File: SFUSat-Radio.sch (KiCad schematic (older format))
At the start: 11 parts, among them J1 SMA, J2 CONN-2POS-0.156\", P1 CONN_02X05, U1 2N7002DW

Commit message: added CC1101, fixed mission symbols
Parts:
- removed J2: CONN-2POS-0.156\", symbol CONN-2POS-0.156"
- added J3: PC104-8BIT, SFUSat:PC104-8bit, symbol PC104-8BIT
- added J4, J5, J6, J7: PC104PTH, SFUSat:PC104PTH, symbol PC104PTH
- D1, D2, D3: footprint SFUSat-Radio:LED_0603 -> SFUSat:LED_0603; symbol LED-RESCUE-SFUSat-Radio -> LED
- J1: footprint (none) -> SFUSat:SMA-Vert-TH
- R1, R2, R3: footprint (none) -> SFUSat:R_0402
- SW?1: footprint (none) -> SFUSat:1877285-2
- U1: footprint (none) -> SFUSat:SOT-363
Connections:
- wire segments 46 -> 52
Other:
- note added: "Need pull-up?\n"
- moved on the sheet: J1
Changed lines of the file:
@@
 F 0 "U1" H 6550 1350 60  0000 C CNN
 F 1 "2N7002DW" H 6350 1850 60  0000 C CNN
-F 2 "" H 6350 1600 60  0001 C CNN
+F 2 "SFUSat:SOT-363" H 6350 1600 60  0001 C CNN
 F 3 "" H 6350 1600 60  0000 C CNN
 	1    6350 1600
@@
 $EndComp
 $Comp
-L LED-RESCUE-SFUSat-Radio D1
+L LED D1
 U 1 1 587E94F9
 P 6950 1250
 F 0 "D1" H 6950 1350 50  0000 C CNN
 F 1 "GREEN" H 6950 1150 50  0000 C CNN
-F 2 "SFUSat-Radio:LED_0603" H 6950 1250 50  0001 C CNN
+F 2 "SFUSat:LED_0603" H 6950 1250 50  0001 C CNN
 F 3 "" H 6950 1250 50  0000 C CNN
 	1    6950 1250
@@
 F 0 "R1" V 7030 900 50  0000 C CNN
 F 1 "287" V 6950 900 50  0000 C CNN
-F 2 "" V 6880 900 50  0001 C CNN
+F 2 "SFUSat:R_0402" V 6880 900 50  0001 C CNN
 F 3 "" H 6950 900 50  0000 C CNN
 	1    6950 900
@@
 F 0 "R2" V 7330 900 50  0000 C CNN
 F 1 "287" V 7250 900 50  0000 C CNN
-F 2 "" V 7180 900 50  0001 C CNN
+F 2 "SFUSat:R_0402" V 7180 900 50  0001 C CNN
 F 3 "" H 7250 900 50  0000 C CNN
 	1    7250 900
@@
 $EndComp
 $Comp
-L LED-RESCUE-SFUSat-Radio D2
+L LED D2
 U 1 1 587EC634
 P 7250 1250
 F 0 "D2" H 7250 1350 50  0000 C CNN
 F 1 "RED" H 7250 1150 50  0000 C CNN
-F 2 "SFUSat-Radio:LED_0603" H 7250 1250 50  0001 C CNN
+F 2 "SFUSat:LED_0603" H 7250 1250 50  0001 C CNN
 F 3 "" H 7250 1250 50  0000 C CNN
 	1    7250 1250
@@
 $EndComp
 $Comp
-L GND #PWR01
+L GND #PWR8
 U 1 1 587EE6E2
 P 6800 1550
-F 0 "#PWR01" H 6800 1300 50  0001 C CNN
+F 0 "#PWR8" H 6800 1300 50  0001 C CNN
 F 1 "GND" H 6800 1400 50  0000 C CNN
 F 2 "" H 6800 1550 50  0000 C CNN
@@
 $EndComp
 $Comp
-L GND #PWR02
+L GND #PWR9
 U 1 1 587EE79C
 P 6800 1750
-F 0 "#PWR02" H 6800 1500 50  0001 C CNN
+F 0 "#PWR9" H 6800 1500 50  0001 C CNN
 F 1 "GND" H 6800 1600 50  0000 C CNN
 F 2 "" H 6800 1750 50  0000 C CNN
@@
 $EndComp
 $Comp
-L LED-RESCUE-SFUSat-Radio D3
+L LED D3
 U 1 1 587F1822
 P 7550 1250
 F 0 "D3" H 7550 1350 50  0000 C CNN
 F 1 "ORANGE" H 7550 1150 50  0000 C CNN
-F 2 "SFUSat-Radio:LED_0603" H 7550 1250 50  0001 C CNN
+F 2 "SFUSat:LED_0603" H 7550 1250 50  0001 C CNN
 F 3 "" H 7550 1250 50  0000 C CNN
 	1    7550 1250
@@
 F 0 "R3" V 7630 900 50  0000 C CNN
 F 1 "287" V 7550 900 50  0000 C CNN
-F 2 "" V 7480 900 50  0001 C CNN
+F 2 "SFUSat:R_0402" V 7480 900 50  0001 C CNN
 F 3 "" H 7550 900 50  0000 C CNN
 	1    7550 900
@@
 $EndComp
 $Comp
-L GND #PWR03
+L GND #PWR10
 U 1 1 587F1A5F
 P 7550 1450
-F 0 "#PWR03" H 7550 1200 50  0001 C CNN
+F 0 "#PWR10" H 7550 1200 50  0001 C CNN
 F 1 "GND" H 7550 1300 50  0000 C CNN
 F 2 "" H 7550 1450 50  0000 C CNN
@@
 L SMA J1
 U 1 1 5883A1B6
-P 9200 5050
-F 0 "J1" H 9400 4900 60  0000 C CNN
-F 1 "SMA" H 9400 5200 60  0000 C CNN
-F 2 "" H 9200 5050 60  0001 C CNN
-F 3 "" H 9200 5050 60  0000 C CNN
-	1    9200 5050
-	1    0    0    -1
-$EndComp
-$Comp
-L GND #PWR04
+P 9150 5100
+F 0 "J1" H 9350 4950 60  0000 C CNN
+F 1 "SMA" H 9350 5250 60  0000 C CNN
+F 2 "SFUSat:SMA-Vert-TH" H 9150 5100 60  0001 C CNN
+F 3 "" H 9150 5100 60  0000 C CNN
+	1    9150 5100
+	1    0    0    -1
+$EndComp
+$Comp
+L GND #PWR11
 U 1 1 5883A521
-P 9700 5050
-F 0 "#PWR04" H 9700 4800 50  0001 C CNN
-F 1 "GND" H 9700 4900 50  0000 C CNN
-F 2 "" H 9700 5050 50  0000 C CNN
-F 3 "" H 9700 5050 50  0000 C CNN
-	1    9700 5050
-	0    -1   -1   0
+P 8700 5200
+F 0 "#PWR11" H 8700 4950 50  0001 C CNN
+F 1 "GND" H 8700 5050 50  0000 C CNN
+F 2 "" H 8700 5200 50  0000 C CNN
+F 3 "" H 8700 5200 50  0000 C CNN
+	1    8700 5200
+	0    1    1    0
 $EndComp
 Text Label 4900 2950 0    60   ~ 0
 OP_3.3
-$Comp
-L CONN-2POS-0.156" J2
-U 1 1 58885286
-P 3925 2700
-F 0 "J2" H 3975 2550 60  0000 C CNN
-F 1 "CONN-2POS-0.156\"" H 3925 2900 60  0000 C CNN
-F 2 "" H 3925 2600 60  0001 C CNN
-F 3 "" H 3925 2600 60  0000 C CNN
-	1    3925 2700
-	1    0    0    -1
-$EndComp
-$Comp
-L GND #PWR05
-U 1 1 58885C3B
-P 4300 2800
-F 0 "#PWR05" H 4300 2550 50  0001 C CNN
-F 1 "GND" H 4300 2650 50  0000 C CNN
-F 2 "" H 4300 2800 50  0000 C CNN
-F 3 "" H 4300 2800 50  0000 C CNN
-	1    4300 2800
-	1    0    0    -1
-$EndComp
 $Comp
 L SPST SW?1
@@
 F 0 "SW?1" H 2450 6000 60  0000 C CNN
 F 1 "SPST" H 2450 5450 60  0000 C CNN
-F 2 "" H 2450 5750 60  0001 C CNN
+F 2 "SFUSat:1877285-2" H 2450 5750 60  0001 C CNN
 F 3 "https://www.digikey.com/product-detail/en/c-k/PTS645SM43SMTR92-LFS/CKN9112CT-ND/1146934" H 2450 5750 60  0001 C CNN
 	1    2450 5750
@@
 OP_3.3
 $Comp
-L GND #PWR06
-U 1 1 59141A1F
-P 1850 5900
-F 0 "#PWR06" H 1850 5650 50  0001 C CNN
-F 1 "GND" H 1850 5750 50  0000 C CNN
-F 2 "" H 1850 5900 50  0000 C CNN
-F 3 "" H 1850 5900 50  0000 C CNN
-	1    1850 5900
-	0    1    1    0
-$EndComp
-$Comp
-L GND #PWR07
+L GND #PWR2
 U 1 1 59141AD5
-P 3050 5900
-F 0 "#PWR07" H 3050 5650 50  0001 C CNN
-F 1 "GND" H 3050 5750 50  0000 C CNN
-F 2 "" H 3050 5900 50  0000 C CNN
-F 3 "" H 3050 5900 50  0000 C CNN
-	1    3050 5900
-	0    -1   -1   0
-$EndComp
-$Comp
-L GND #PWR08
+P 2750 5850
+F 0 "#PWR2" H 2750 5600 50  0001 C CNN
+F 1 "GND" H 2750 5700 50  0000 C CNN
+F 2 "" H 2750 5850 50  0000 C CNN
+F 3 "" H 2750 5850 50  0000 C CNN
+	1    2750 5850
+	0    -1   -1   0
+$EndComp
+$Comp
+L GND #PWR1
 U 1 1 587CE076
 P 1250 4800
-F 0 "#PWR08" H 1250 4550 50  0001 C CNN
+F 0 "#PWR1" H 1250 4550 50  0001 C CNN
 F 1 "GND" H 1250 4650 50  0000 C CNN
 F 2 "" H 1250 4800 50  0000 C CNN
@@
 	1650 5200 1250 5200
 Wire Wire Line
-	3000 5900 3050 5900
-Wire Wire Line
-	1850 5900 1900 5900
-Wire Wire Line
-	3000 5550 3000 5600
-Wire Wire Line
-	1900 5550 3000 5550
-Wire Wire Line
-	1900 5600 1900 5550
-Wire Wire Line
-	4300 2750 4300 2800
-Wire Wire Line
-	4225 2750 4300 2750
-Wire Wire Line
 	5400 2950 4900 2950
-Wire Wire Line
-	3000 5600 3700 5600
 Wire Wire Line
 	3700 5350 3400 5350
@@
 	5500 1500 5900 1500
 Wire Wire Line
-	7250 1650 7250 1450
-Wire Wire Line
-	6800 1650 7250 1650
+	7250 1400 7250 1650
+Wire Wire Line
+	7250 1650 6800 1650
 Wire Wire Line
 	6800 1450 6950 1450
@@
 	5200 4600 6050 4600
 Wire Wire Line
-	8100 5050 8700 5050
+	8100 5050 8850 5050
 $Comp
 L CONN_02X05 P1
@@
 	1    0    0    -1
 $EndComp
+$Comp
+L PC104-8BIT J3
+U 1 1 59239648
+P 1750 2500
+F 0 "J3" H 2000 850 60  0000 C CNN
+F 1 "PC104-8BIT" H 1700 4250 60  0000 C CNN
+F 2 "SFUSat:PC104-8bit" H 1750 3500 60  0001 C CNN
+F 3 "" H 1750 3500 60  0001 C CNN
+	1    1750 2500
+	1    0    0    -1
+$EndComp
+$Comp
+L PC104PTH J4
+U 1 1 5923A0F7
+P 3500 900
+F 0 "J4" H 3500 750 60  0000 C CNN
+F 1 "PC104PTH" H 3500 1050 60  0000 C CNN
+F 2 "SFUSat:PC104PTH" H 3500 900 60  0001 C CNN
+F 3 "" H 3500 900 60  0001 C CNN
+	1    3500 900
+	1    0    0    -1
+$EndComp
+$Comp
+L PC104PTH J5
+U 1 1 5923A1D0
+P 3500 1300
+F 0 "J5" H 3500 1150 60  0000 C CNN
+F 1 "PC104PTH" H 3500 1450 60  0000 C CNN
+F 2 "SFUSat:PC104PTH" H 3500 1300 60  0001 C CNN
+F 3 "" H 3500 1300 60  0001 C CNN
+	1    3500 1300
+	1    0    0    -1
+$EndComp
+$Comp
+L PC104PTH J6
+U 1 1 5923A28B
+P 3500 1700
+F 0 "J6" H 3500 1550 60  0000 C CNN
+F 1 "PC104PTH" H 3500 1850 60  0000 C CNN
+F 2 "SFUSat:PC104PTH" H 3500 1700 60  0001 C CNN
+F 3 "" H 3500 1700 60  0001 C CNN
+	1    3500 1700
+	1    0    0    -1
+$EndComp
+$Comp
+L PC104PTH J7
+U 1 1 5923A34C
+P 3500 2100
+F 0 "J7" H 3500 1950 60  0000 C CNN
+F 1 "PC104PTH" H 3500 2250 60  0000 C CNN
+F 2 "SFUSat:PC104PTH" H 3500 2100 60  0001 C CNN
+F 3 "" H 3500 2100 60  0001 C CNN
+	1    3500 2100
+	1    0    0    -1
+$EndComp
+$Comp
+L GND #PWR3
+U 1 1 5923AA11
+P 3150 900
+F 0 "#PWR3" H 3150 650 50  0001 C CNN
+F 1 "GND" H 3150 750 50  0000 C CNN
+F 2 "" H 3150 900 50  0001 C CNN
+F 3 "" H 3150 900 50  0001 C CNN
+	1    3150 900
+	0    1    1    0
+$EndComp
+$Comp
+L GND #PWR4
+U 1 1 5923ACCD
+P 3150 1300
+F 0 "#PWR4" H 3150 1050 50  0001 C CNN
+F 1 "GND" H 3150 1150 50  0000 C CNN
+F 2 "" H 3150 1300 50  0001 C CNN
+F 3 "" H 3150 1300 50  0001 C CNN
+	1    3150 1300
+	0    1    1    0
+$EndComp
+$Comp
+L GND #PWR5
+U 1 1 5923AD8B
+P 3150 1700
+F 0 "#PWR5" H 3150 1450 50  0001 C CNN
+F 1 "GND" H 3150 1550 50  0000 C CNN
+F 2 "" H 3150 1700 50  0001 C CNN
+F 3 "" H 3150 1700 50  0001 C CNN
+	1    3150 1700
+	0    1    1    0
+$EndComp
+$Comp
+L GND #PWR6
+U 1 1 5923B09C
+P 3150 2100
+F 0 "#PWR6" H 3150 1850 50  0001 C CNN
+F 1 "GND" H 3150 1950 50  0000 C CNN
+F 2 "" H 3150 2100 50  0001 C CNN
+F 3 "" H 3150 2100 50  0001 C CNN
+	1    3150 2100
+	0    1    1    0
+$EndComp
+Wire Wire Line
+	3150 900  3200 900
+Wire Wire Line
+	3200 1300 3150 1300
+Wire Wire Line
+	3150 1700 3200 1700
+Wire Wire Line
+	3200 2100 3150 2100
+Wire Wire Line
+	3700 5600 2650 5600
+Wire Wire Line
+	2650 5600 2650 5650
+Wire Wire Line
+	2650 5650 2250 5650
+Wire Wire Line
+	2250 5850 2750 5850
+Connection ~ 2650 5850
+Text Notes 2750 6050 0    60   ~ 0
+Need pull-up?\n
+Wire Wire Line
+	8850 5200 8700 5200
+Wire Wire Line
+	6950 1050 6950 1100
+Wire Wire Line
+	6950 1450 6950 1400
+Wire Wire Line
+	7250 1100 7250 1050
+Wire Wire Line
+	7550 1050 7550 1100
+Wire Wire Line
+	7550 1400 7550 1450
 $EndSCHEMATC

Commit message: Started added CC1101-Q1 components
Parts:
- J1: symbol SMA -> SMA-RESCUE-SFUSat-Radio
- SW?1: symbol SPST -> SPST-RESCUE-SFUSat-Radio
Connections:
- net labels added: ~CS, ~RESET
- net labels removed: CSn, RESET_N
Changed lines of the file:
@@
 EESchema Schematic File Version 2
+LIBS:SFUSat-Radio-rescue
 LIBS:power
 LIBS:device
@@
 LIBS:valves
 LIBS:SFUSat
+LIBS:SFUSat-Radio-cache
 EELAYER 25 0
 EELAYER END
@@
 F0 "Transceiver" 60
 F1 "Transceiver.sch" 60
-F2 "RESET" I L 3700 5600 60
+F2 "~RESET" I L 3700 5600 60
 F3 "GPIO2" I L 3700 4050 60
 F4 "MOSI" I L 3700 4850 60
 F5 "SCLK" I L 3700 4600 60
 F6 "MISO" I L 3700 5100 60
-F7 "CSN" I L 3700 5350 60
+F7 "~CS" I L 3700 5350 60
 F8 "RX" I R 5200 4600 60
 F9 "TX" I R 5200 4900 60
@@
 GPIO2
 Text Label 1250 5000 0    60   ~ 0
-CSn
+~CS
 Text Label 1250 5100 0    60   ~ 0
-RESET_N
+~RESET
 Text Label 3400 3800 0    60   ~ 0
 GPIO0
@@
 MISO
 Text Label 3400 5350 0    60   ~ 0
-CSn
+~CS
 Text Label 3400 5600 0    60   ~ 0
-RESET_N
-$Comp
-L SMA J1
+~RESET
+$Comp
+L SMA-RESCUE-SFUSat-Radio J1
 U 1 1 5883A1B6
 P 9150 5100
@@
 OP_3.3
 $Comp
-L SPST SW?1
+L SPST-RESCUE-SFUSat-Radio SW?1
 U 1 1 5913F847
 P 2450 5750

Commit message: fixed rescue library
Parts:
- J1: symbol SMA-RESCUE-SFUSat-Radio -> SMA
- P1: footprint (none) -> SFUSat:Socket_Strip_Straight_2x05
- SW1: renamed from SW?1; footprint SFUSat:1877285-2 -> SFUSat:PTS645SMT; symbol SPST-RESCUE-SFUSat-Radio -> SPST
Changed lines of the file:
@@
 EESchema Schematic File Version 2
-LIBS:SFUSat-Radio-rescue
 LIBS:power
 LIBS:device
@@
 $EndComp
 $Comp
-L GND #PWR8
+L GND #PWR01
 U 1 1 587EE6E2
 P 6800 1550
-F 0 "#PWR8" H 6800 1300 50  0001 C CNN
+F 0 "#PWR01" H 6800 1300 50  0001 C CNN
 F 1 "GND" H 6800 1400 50  0000 C CNN
 F 2 "" H 6800 1550 50  0000 C CNN
@@
 $EndComp
 $Comp
-L GND #PWR9
+L GND #PWR02
 U 1 1 587EE79C
 P 6800 1750
-F 0 "#PWR9" H 6800 1500 50  0001 C CNN
+F 0 "#PWR02" H 6800 1500 50  0001 C CNN
 F 1 "GND" H 6800 1600 50  0000 C CNN
 F 2 "" H 6800 1750 50  0000 C CNN
@@
 $EndComp
 $Comp
-L GND #PWR10
+L GND #PWR03
 U 1 1 587F1A5F
 P 7550 1450
-F 0 "#PWR10" H 7550 1200 50  0001 C CNN
+F 0 "#PWR03" H 7550 1200 50  0001 C CNN
 F 1 "GND" H 7550 1300 50  0000 C CNN
 F 2 "" H 7550 1450 50  0000 C CNN
@@
 ~RESET
 $Comp
-L SMA-RESCUE-SFUSat-Radio J1
+L SMA J1
 U 1 1 5883A1B6
 P 9150 5100
@@
 $EndComp
 $Comp
-L GND #PWR11
+L GND #PWR04
 U 1 1 5883A521
 P 8700 5200
-F 0 "#PWR11" H 8700 4950 50  0001 C CNN
+F 0 "#PWR04" H 8700 4950 50  0001 C CNN
 F 1 "GND" H 8700 5050 50  0000 C CNN
 F 2 "" H 8700 5200 50  0000 C CNN
@@
 OP_3.3
 $Comp
-L SPST-RESCUE-SFUSat-Radio SW?1
+L SPST SW1
 U 1 1 5913F847
 P 2450 5750
-F 0 "SW?1" H 2450 6000 60  0000 C CNN
+F 0 "SW1" H 2450 6000 60  0000 C CNN
 F 1 "SPST" H 2450 5450 60  0000 C CNN
-F 2 "SFUSat:1877285-2" H 2450 5750 60  0001 C CNN
+F 2 "SFUSat:PTS645SMT" H 2450 5750 60  0001 C CNN
 F 3 "https://www.digikey.com/product-detail/en/c-k/PTS645SM43SMTR92-LFS/CKN9112CT-ND/1146934" H 2450 5750 60  0001 C CNN
 	1    2450 5750
@@
 OP_3.3
 $Comp
-L GND #PWR2
+L GND #PWR05
 U 1 1 59141AD5
 P 2750 5850
-F 0 "#PWR2" H 2750 5600 50  0001 C CNN
+F 0 "#PWR05" H 2750 5600 50  0001 C CNN
 F 1 "GND" H 2750 5700 50  0000 C CNN
 F 2 "" H 2750 5850 50  0000 C CNN
@@
 $EndComp
 $Comp
-L GND #PWR1
+L GND #PWR06
 U 1 1 587CE076
 P 1250 4800
-F 0 "#PWR1" H 1250 4550 50  0001 C CNN
+F 0 "#PWR06" H 1250 4550 50  0001 C CNN
 F 1 "GND" H 1250 4650 50  0000 C CNN
 F 2 "" H 1250 4800 50  0000 C CNN
@@
 F 0 "P1" H 1900 5300 50  0000 C CNN
 F 1 "CONN_02X05" H 1900 4700 50  0000 C CNN
-F 2 "" H 1900 3800 50  0001 C CNN
+F 2 "SFUSat:Socket_Strip_Straight_2x05" H 1900 3800 50  0001 C CNN
 F 3 "" H 1900 3800 50  0000 C CNN
 	1    1900 5000
@@
 $EndComp
 $Comp
-L GND #PWR3
+L GND #PWR07
 U 1 1 5923AA11
 P 3150 900
-F 0 "#PWR3" H 3150 650 50  0001 C CNN
+F 0 "#PWR07" H 3150 650 50  0001 C CNN
 F 1 "GND" H 3150 750 50  0000 C CNN
 F 2 "" H 3150 900 50  0001 C CNN
@@
 $EndComp
 $Comp
-L GND #PWR4
+L GND #PWR08
 U 1 1 5923ACCD
 P 3150 1300
-F 0 "#PWR4" H 3150 1050 50  0001 C CNN
+F 0 "#PWR08" H 3150 1050 50  0001 C CNN
 F 1 "GND" H 3150 1150 50  0000 C CNN
 F 2 "" H 3150 1300 50  0001 C CNN
@@
 $EndComp
 $Comp
-L GND #PWR5
+L GND #PWR09
 U 1 1 5923AD8B
 P 3150 1700
-F 0 "#PWR5" H 3150 1450 50  0001 C CNN
+F 0 "#PWR09" H 3150 1450 50  0001 C CNN
 F 1 "GND" H 3150 1550 50  0000 C CNN
 F 2 "" H 3150 1700 50  0001 C CNN
@@
 $EndComp
 $Comp
-L GND #PWR6
+L GND #PWR010
 U 1 1 5923B09C
 P 3150 2100
-F 0 "#PWR6" H 3150 1850 50  0001 C CNN
+F 0 "#PWR010" H 3150 1850 50  0001 C CNN
 F 1 "GND" H 3150 1950 50  0000 C CNN
 F 2 "" H 3150 2100 50  0001 C CNN

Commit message: Removed SW1
CC1101-Q1 has no reset pin, so no point in having a reset switch
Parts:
- removed SW1: SPST, SFUSat:PTS645SMT, symbol SPST
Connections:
- wire segments 52 -> 48
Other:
- note removed: "Need pull-up?\n"
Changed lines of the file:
@@
 F0 "Transceiver" 60
 F1 "Transceiver.sch" 60
-F2 "~RESET" I L 3700 5600 60
-F3 "GPIO2" I L 3700 4050 60
-F4 "MOSI" I L 3700 4850 60
-F5 "SCLK" I L 3700 4600 60
-F6 "MISO" I L 3700 5100 60
-F7 "~CS" I L 3700 5350 60
-F8 "RX" I R 5200 4600 60
-F9 "TX" I R 5200 4900 60
-F10 "3V3" I R 5200 4125 60
-F11 "TRX_SIG" I R 5200 5250 60
-F12 "GPIO0" I L 3700 3800 60
+F2 "GPIO2" I L 3700 4050 60
+F3 "MOSI" I L 3700 4850 60
+F4 "SCLK" I L 3700 4600 60
+F5 "MISO" I L 3700 5100 60
+F6 "~CS" I L 3700 5350 60
+F7 "RX" I R 5200 4600 60
+F8 "TX" I R 5200 4900 60
+F9 "3V3" I R 5200 4125 60
+F10 "TRX_SIG" I R 5200 5250 60
+F11 "GPIO0" I L 3700 3800 60
 $EndSheet
 $Sheet
@@
 Text Label 3400 5350 0    60   ~ 0
 ~CS
-Text Label 3400 5600 0    60   ~ 0
-~RESET
 $Comp
 L SMA J1
@@
 Text Label 4900 2950 0    60   ~ 0
 OP_3.3
-$Comp
-L SPST SW1
-U 1 1 5913F847
-P 2450 5750
-F 0 "SW1" H 2450 6000 60  0000 C CNN
-F 1 "SPST" H 2450 5450 60  0000 C CNN
-F 2 "SFUSat:PTS645SMT" H 2450 5750 60  0001 C CNN
-F 3 "https://www.digikey.com/product-detail/en/c-k/PTS645SM43SMTR92-LFS/CKN9112CT-ND/1146934" H 2450 5750 60  0001 C CNN
-	1    2450 5750
-	1    0    0    -1
-$EndComp
 Text Label 1250 5200 0    60   ~ 0
 OP_3.3
-$Comp
-L GND #PWR05
-U 1 1 59141AD5
-P 2750 5850
-F 0 "#PWR05" H 2750 5600 50  0001 C CNN
-F 1 "GND" H 2750 5700 50  0000 C CNN
-F 2 "" H 2750 5850 50  0000 C CNN
-F 3 "" H 2750 5850 50  0000 C CNN
-	1    2750 5850
-	0    -1   -1   0
-$EndComp
 $Comp
 L GND #PWR06
@@
 	3200 2100 3150 2100
 Wire Wire Line
-	3700 5600 2650 5600
-Wire Wire Line
-	2650 5600 2650 5650
-Wire Wire Line
-	2650 5650 2250 5650
-Wire Wire Line
-	2250 5850 2750 5850
-Connection ~ 2650 5850
-Text Notes 2750 6050 0    60   ~ 0
-Need pull-up?\n
-Wire Wire Line
 	8850 5200 8700 5200

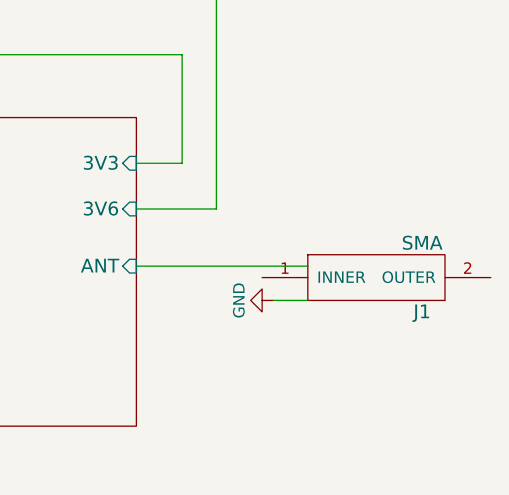
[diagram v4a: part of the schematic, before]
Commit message: Renumbered reference designators
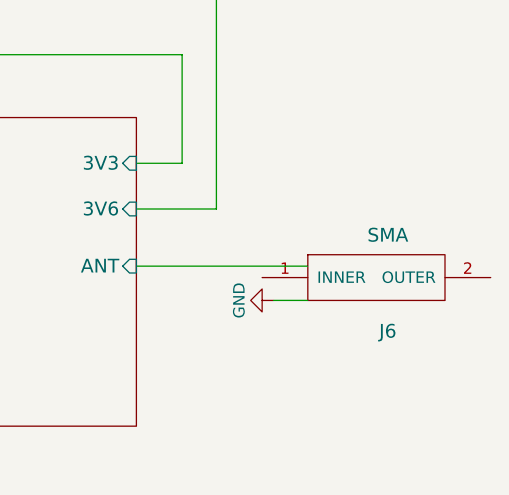
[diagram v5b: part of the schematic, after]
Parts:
- renumbered J3 to J1, J4 to J2, J5 to J3, J6 to J4, J7 to J5, J1 to J6
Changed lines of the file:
@@
 ~CS
 $Comp
-L SMA J1
+L SMA J6
 U 1 1 5883A1B6
 P 9150 5100
-F 0 "J1" H 9350 4950 60  0000 C CNN
-F 1 "SMA" H 9350 5250 60  0000 C CNN
+F 0 "J6" H 9200 4900 60  0000 C TNN
+F 1 "SMA" H 9200 5250 60  0000 C BNN
 F 2 "SFUSat:SMA-Vert-TH" H 9150 5100 60  0001 C CNN
 F 3 "" H 9150 5100 60  0000 C CNN
@@
 OP_3.3
 $Comp
-L GND #PWR06
+L GND #PWR05
 U 1 1 587CE076
 P 1250 4800
-F 0 "#PWR06" H 1250 4550 50  0001 C CNN
+F 0 "#PWR05" H 1250 4550 50  0001 C CNN
 F 1 "GND" H 1250 4650 50  0000 C CNN
 F 2 "" H 1250 4800 50  0000 C CNN
@@
 $EndComp
 $Comp
-L PC104-8BIT J3
+L PC104-8BIT J1
 U 1 1 59239648
 P 1750 2500
-F 0 "J3" H 2000 850 60  0000 C CNN
+F 0 "J1" H 2000 850 60  0000 C CNN
 F 1 "PC104-8BIT" H 1700 4250 60  0000 C CNN
 F 2 "SFUSat:PC104-8bit" H 1750 3500 60  0001 C CNN
@@
 $EndComp
 $Comp
-L PC104PTH J4
+L PC104PTH J2
 U 1 1 5923A0F7
 P 3500 900
-F 0 "J4" H 3500 750 60  0000 C CNN
+F 0 "J2" H 3500 750 60  0000 C CNN
 F 1 "PC104PTH" H 3500 1050 60  0000 C CNN
 F 2 "SFUSat:PC104PTH" H 3500 900 60  0001 C CNN
@@
 $EndComp
 $Comp
-L PC104PTH J5
+L PC104PTH J3
 U 1 1 5923A1D0
 P 3500 1300
-F 0 "J5" H 3500 1150 60  0000 C CNN
+F 0 "J3" H 3500 1150 60  0000 C CNN
 F 1 "PC104PTH" H 3500 1450 60  0000 C CNN
 F 2 "SFUSat:PC104PTH" H 3500 1300 60  0001 C CNN
@@
 $EndComp
 $Comp
-L PC104PTH J6
+L PC104PTH J4
 U 1 1 5923A28B
 P 3500 1700
-F 0 "J6" H 3500 1550 60  0000 C CNN
+F 0 "J4" H 3500 1550 60  0000 C CNN
 F 1 "PC104PTH" H 3500 1850 60  0000 C CNN
 F 2 "SFUSat:PC104PTH" H 3500 1700 60  0001 C CNN
@@
 $EndComp
 $Comp
-L PC104PTH J7
+L PC104PTH J5
 U 1 1 5923A34C
 P 3500 2100
-F 0 "J7" H 3500 1950 60  0000 C CNN
+F 0 "J5" H 3500 1950 60  0000 C CNN
 F 1 "PC104PTH" H 3500 2250 60  0000 C CNN
 F 2 "SFUSat:PC104PTH" H 3500 2100 60  0001 C CNN
@@
 $EndComp
 $Comp
-L GND #PWR07
+L GND #PWR06
 U 1 1 5923AA11
 P 3150 900
-F 0 "#PWR07" H 3150 650 50  0001 C CNN
+F 0 "#PWR06" H 3150 650 50  0001 C CNN
 F 1 "GND" H 3150 750 50  0000 C CNN
 F 2 "" H 3150 900 50  0001 C CNN
@@
 $EndComp
 $Comp
-L GND #PWR08
+L GND #PWR07
 U 1 1 5923ACCD
 P 3150 1300
-F 0 "#PWR08" H 3150 1050 50  0001 C CNN
+F 0 "#PWR07" H 3150 1050 50  0001 C CNN
 F 1 "GND" H 3150 1150 50  0000 C CNN
 F 2 "" H 3150 1300 50  0001 C CNN
@@
 $EndComp
 $Comp
-L GND #PWR09
+L GND #PWR08
 U 1 1 5923AD8B
 P 3150 1700
-F 0 "#PWR09" H 3150 1450 50  0001 C CNN
+F 0 "#PWR08" H 3150 1450 50  0001 C CNN
 F 1 "GND" H 3150 1550 50  0000 C CNN
 F 2 "" H 3150 1700 50  0001 C CNN
@@
 $EndComp
 $Comp
-L GND #PWR010
+L GND #PWR09
 U 1 1 5923B09C
 P 3150 2100
-F 0 "#PWR010" H 3150 1850 50  0001 C CNN
+F 0 "#PWR09" H 3150 1850 50  0001 C CNN
 F 1 "GND" H 3150 1950 50  0000 C CNN
 F 2 "" H 3150 2100 50  0001 C CNN
